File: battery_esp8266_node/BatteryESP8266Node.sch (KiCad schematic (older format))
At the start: 17 parts, among them J1 Power, J2 UART, J3 IO Header, SW1 Reset, SW2 Flash, U1 ESP-12E, U2 AP2112K-3.3

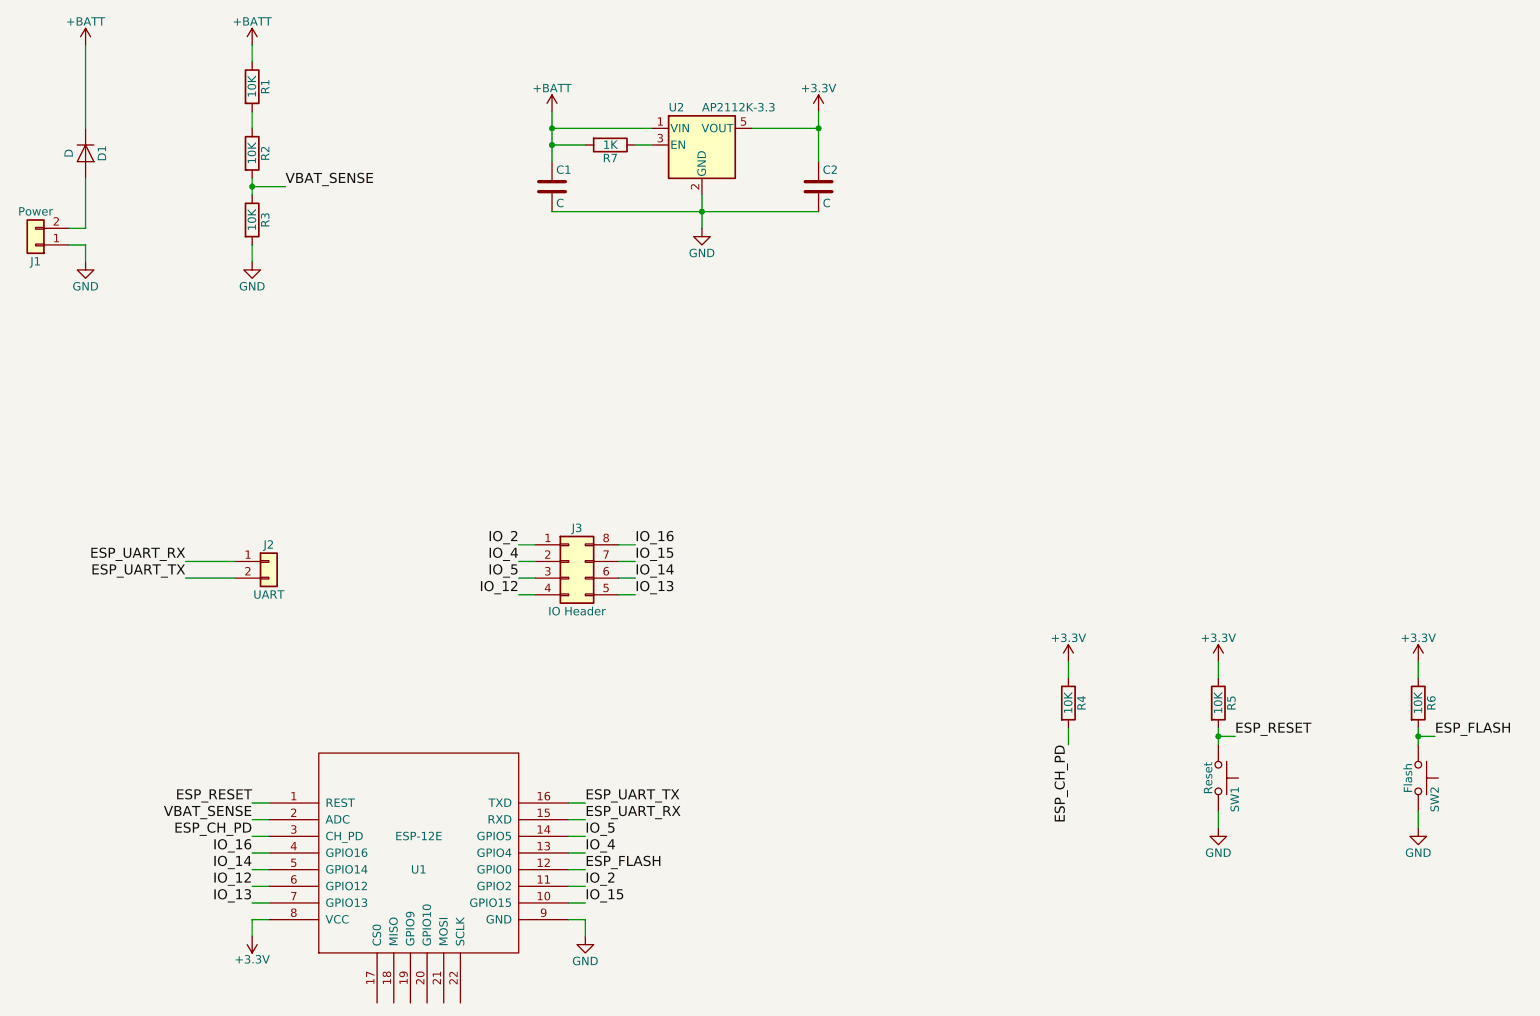
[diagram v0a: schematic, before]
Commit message: Second board revision
All components on a single side, generally neater layout, added proto
headers.
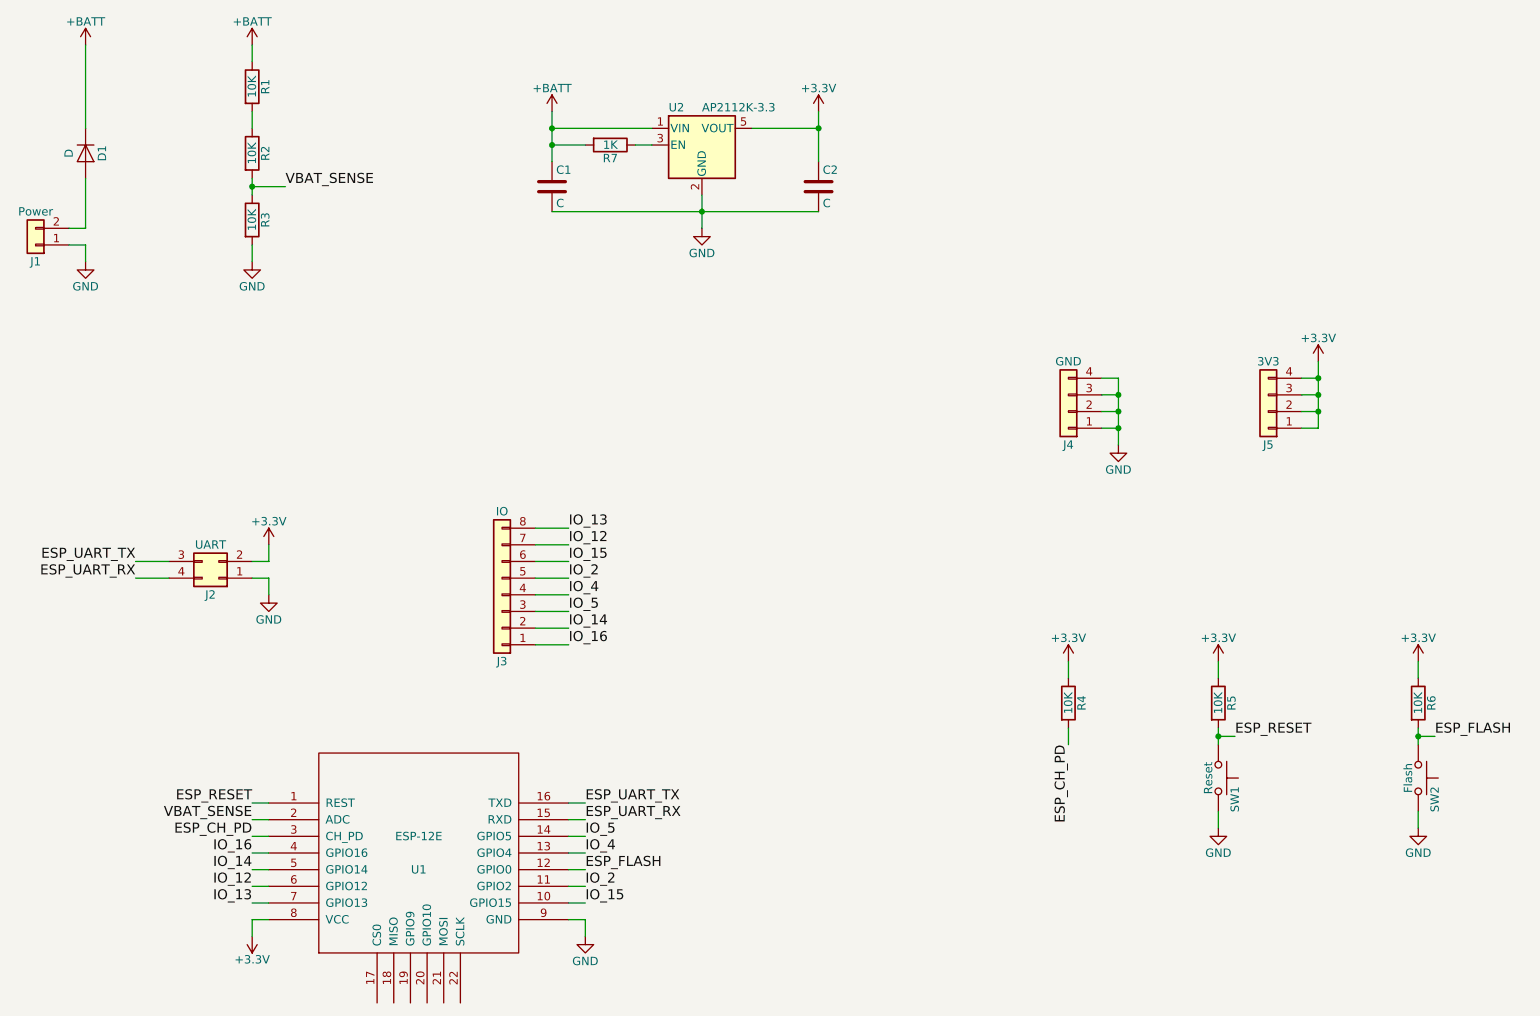
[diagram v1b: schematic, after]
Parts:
- removed J2: UART, Pin_Headers:Pin_Header_Straight_1x02_Pitch2.54mm, symbol Conn_01x02
- removed J3: IO Header, Pin_Headers:Pin_Header_Straight_2x04_Pitch2.54mm, symbol Conn_02x04_Counter_Clockwise
- added J2: UART, Pin_Headers:Pin_Header_Straight_2x02_Pitch2.54mm, symbol Conn_02x02_Counter_Clockwise
- added J3: IO, Pin_Headers:Pin_Header_Straight_1x08_Pitch2.54mm, symbol Conn_01x08
- added J4: GND, Pin_Headers:Pin_Header_Straight_1x04_Pitch2.54mm, symbol Conn_01x04
- added J5: 3V3, Pin_Headers:Pin_Header_Straight_1x04_Pitch2.54mm, symbol Conn_01x04
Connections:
- net +3V3: now also J2.2 (Pin_2), J5.1 (Pin_1), J5.2 (Pin_2), J5.3 (Pin_3), J5.4 (Pin_4)
- net ESP_UART_RX: now also J2.4 (Pin_4)
- net ESP_UART_TX: now also J2.3 (Pin_3)
- net GND: now also J2.1 (Pin_1), J4.1 (Pin_1), J4.2 (Pin_2), J4.3 (Pin_3), J4.4 (Pin_4)
- net IO_12: now also J3.7 (Pin_7)
- net IO_13: now also J3.8 (Pin_8)
- net IO_14: now also J3.2 (Pin_2)
- net IO_15: now also J3.6 (Pin_6)
- net IO_16: now also J3.1 (Pin_1)
- net IO_2: now also J3.5 (Pin_5)
- net IO_4: now also J3.4 (Pin_4)
- net IO_5: now also J3.3 (Pin_3)
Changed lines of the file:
@@
 LIBS:contrib
 LIBS:valves
+LIBS:regulators
 LIBS:ESP8266
-LIBS:regulators
 LIBS:BatteryESP8266Node-cache
 EELAYER 25 0
@@
 Text Label 2600 6350 2    60   ~ 0
 IO_13
-$Comp
-L Conn_02x04_Counter_Clockwise J3
-U 1 1 5A023CD8
-P 4500 4300
-F 0 "J3" H 4550 4500 50  0000 C CNN
-F 1 "IO Header" H 4550 4000 50  0000 C CNN
-F 2 "Pin_Headers:Pin_Header_Straight_2x04_Pitch2.54mm" H 4500 4300 50  0001 C CNN
-F 3 "" H 4500 4300 50  0001 C CNN
-	1    4500 4300
-	1    0    0    -1
-$EndComp
-Text Label 4200 4400 2    60   ~ 0
+Text Label 4500 4600 0    60   ~ 0
 IO_5
-Text Label 4200 4200 2    60   ~ 0
+Text Label 4500 4400 0    60   ~ 0
 IO_2
-Text Label 4200 4300 2    60   ~ 0
+Text Label 4500 4500 0    60   ~ 0
 IO_4
-Text Label 4200 4500 2    60   ~ 0
+Text Label 4500 4200 0    60   ~ 0
 IO_12
-Text Label 4900 4500 0    60   ~ 0
+Text Label 4500 4100 0    60   ~ 0
 IO_13
-Text Label 4900 4400 0    60   ~ 0
+Text Label 4500 4700 0    60   ~ 0
 IO_14
-Text Label 4900 4300 0    60   ~ 0
+Text Label 4500 4300 0    60   ~ 0
 IO_15
-Text Label 4900 4200 0    60   ~ 0
+Text Label 4500 4800 0    60   ~ 0
 IO_16
-Text Label 2200 4400 2    60   ~ 0
+Text Label 1900 4300 2    60   ~ 0
 ESP_UART_TX
-Text Label 2200 4300 2    60   ~ 0
+Text Label 1900 4400 2    60   ~ 0
 ESP_UART_RX
 $Comp
@@
 	4600 6350 4500 6350
 Wire Wire Line
-	4200 4200 4300 4200
-Wire Wire Line
-	4200 4300 4300 4300
-Wire Wire Line
-	4200 4400 4300 4400
-Wire Wire Line
-	4300 4500 4200 4500
-Wire Wire Line
-	4900 4300 4800 4300
-Wire Wire Line
-	4800 4200 4900 4200
-Wire Wire Line
-	4800 4400 4900 4400
-Wire Wire Line
-	4900 4500 4800 4500
-Wire Wire Line
 	2600 1200 2600 1300
 Wire Wire Line
@@
 Wire Wire Line
 	1600 1200 1600 1700
-Wire Wire Line
-	2200 4300 2500 4300
-Wire Wire Line
-	2200 4400 2500 4400
 $Comp
 L ESP-12E U1
@@
 $EndComp
 $Comp
-L Conn_01x02 J2
-U 1 1 5A0A2AF2
-P 2700 4300
-F 0 "J2" H 2700 4400 50  0000 C CNN
-F 1 "UART" H 2700 4100 50  0000 C CNN
-F 2 "Pin_Headers:Pin_Header_Straight_1x02_Pitch2.54mm" H 2700 4300 50  0001 C CNN
-F 3 "" H 2700 4300 50  0001 C CNN
-	1    2700 4300
-	1    0    0    -1
-$EndComp
+L +3.3V #PWR015
+U 1 1 5A106DEF
+P 2700 4200
+F 0 "#PWR015" H 2700 4050 50  0001 C CNN
+F 1 "+3.3V" H 2700 4340 50  0000 C CNN
+F 2 "" H 2700 4200 50  0001 C CNN
+F 3 "" H 2700 4200 50  0001 C CNN
+	1    2700 4200
+	1    0    0    -1
+$EndComp
+$Comp
+L GND #PWR016
+U 1 1 5A106E36
+P 2700 4500
+F 0 "#PWR016" H 2700 4250 50  0001 C CNN
+F 1 "GND" H 2700 4350 50  0000 C CNN
+F 2 "" H 2700 4500 50  0001 C CNN
+F 3 "" H 2700 4500 50  0001 C CNN
+	1    2700 4500
+	1    0    0    -1
+$EndComp
+$Comp
+L Conn_01x08 J3
+U 1 1 5A107287
+P 4100 4500
+F 0 "J3" H 4100 4900 50  0000 C CNN
+F 1 "IO" H 4100 4000 50  0000 C CNN
+F 2 "Pin_Headers:Pin_Header_Straight_1x08_Pitch2.54mm" H 4100 4500 50  0001 C CNN
+F 3 "" H 4100 4500 50  0001 C CNN
+	1    4100 4500
+	-1   0    0    1
+$EndComp
+Wire Wire Line
+	4300 4100 4500 4100
+Wire Wire Line
+	4500 4200 4300 4200
+Wire Wire Line
+	4300 4300 4500 4300
+Wire Wire Line
+	4500 4800 4300 4800
+Wire Wire Line
+	4300 4700 4500 4700
+Wire Wire Line
+	4500 4600 4300 4600
+Wire Wire Line
+	4300 4500 4500 4500
+Wire Wire Line
+	4300 4400 4500 4400
+$Comp
+L Conn_01x04 J4
+U 1 1 5A10822F
+P 7500 3400
+F 0 "J4" H 7500 3600 50  0000 C CNN
+F 1 "GND" H 7500 3100 50  0000 C CNN
+F 2 "Pin_Headers:Pin_Header_Straight_1x04_Pitch2.54mm" H 7500 3400 50  0001 C CNN
+F 3 "" H 7500 3400 50  0001 C CNN
+	1    7500 3400
+	-1   0    0    1
+$EndComp
+$Comp
+L Conn_01x04 J5
+U 1 1 5A1083A8
+P 8700 3400
+F 0 "J5" H 8700 3600 50  0000 C CNN
+F 1 "3V3" H 8700 3100 50  0000 C CNN
+F 2 "Pin_Headers:Pin_Header_Straight_1x04_Pitch2.54mm" H 8700 3400 50  0001 C CNN
+F 3 "" H 8700 3400 50  0001 C CNN
+	1    8700 3400
+	-1   0    0    1
+$EndComp
+$Comp
+L GND #PWR017
+U 1 1 5A108441
+P 7800 3600
+F 0 "#PWR017" H 7800 3350 50  0001 C CNN
+F 1 "GND" H 7800 3450 50  0000 C CNN
+F 2 "" H 7800 3600 50  0001 C CNN
+F 3 "" H 7800 3600 50  0001 C CNN
+	1    7800 3600
+	1    0    0    -1
+$EndComp
+$Comp
+L +3.3V #PWR018
+U 1 1 5A10847B
+P 9000 3100
+F 0 "#PWR018" H 9000 2950 50  0001 C CNN
+F 1 "+3.3V" H 9000 3240 50  0000 C CNN
+F 2 "" H 9000 3100 50  0001 C CNN
+F 3 "" H 9000 3100 50  0001 C CNN
+	1    9000 3100
+	1    0    0    -1
+$EndComp
+Wire Wire Line
+	7700 3200 7800 3200
+Wire Wire Line
+	7800 3200 7800 3600
+Wire Wire Line
+	7700 3500 7800 3500
+Connection ~ 7800 3500
+Wire Wire Line
+	7700 3400 7800 3400
+Connection ~ 7800 3400
+Wire Wire Line
+	7700 3300 7800 3300
+Connection ~ 7800 3300
+Wire Wire Line
+	9000 3100 9000 3500
+Wire Wire Line
+	9000 3500 8900 3500
+Wire Wire Line
+	8900 3400 9000 3400
+Connection ~ 9000 3400
+Wire Wire Line
+	8900 3300 9000 3300
+Connection ~ 9000 3300
+Wire Wire Line
+	8900 3200 9000 3200
+Connection ~ 9000 3200
+$Comp
+L Conn_02x02_Counter_Clockwise J2
+U 1 1 5A108D38
+P 2400 4400
+F 0 "J2" H 2450 4500 50  0000 C CNN
+F 1 "UART" H 2450 4200 50  0000 C CNN
+F 2 "Pin_Headers:Pin_Header_Straight_2x02_Pitch2.54mm" H 2400 4400 50  0001 C CNN
+F 3 "" H 2400 4400 50  0001 C CNN
+	1    2400 4400
+	-1   0    0    1
+$EndComp
+Wire Wire Line
+	2600 4400 2700 4400
+Wire Wire Line
+	2700 4400 2700 4500
+Wire Wire Line
+	2700 4200 2700 4300
+Wire Wire Line
+	2700 4300 2600 4300
+Wire Wire Line
+	2100 4300 1900 4300
+Wire Wire Line
+	1900 4400 2100 4400
 $EndSCHEMATC
